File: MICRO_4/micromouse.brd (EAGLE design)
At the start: 100 x 80 mm, 33 parts

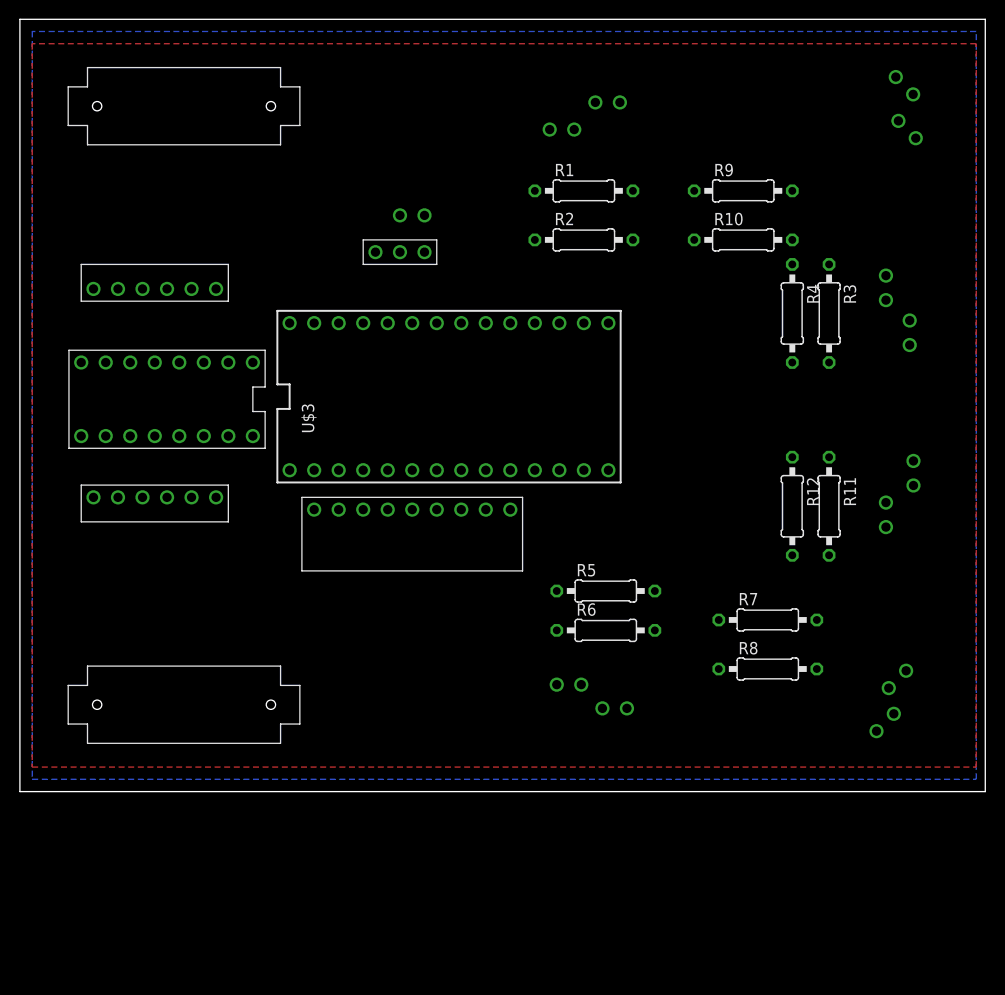
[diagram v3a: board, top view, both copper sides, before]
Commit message: all the traces on top layer alone next will include bottom layer for traces
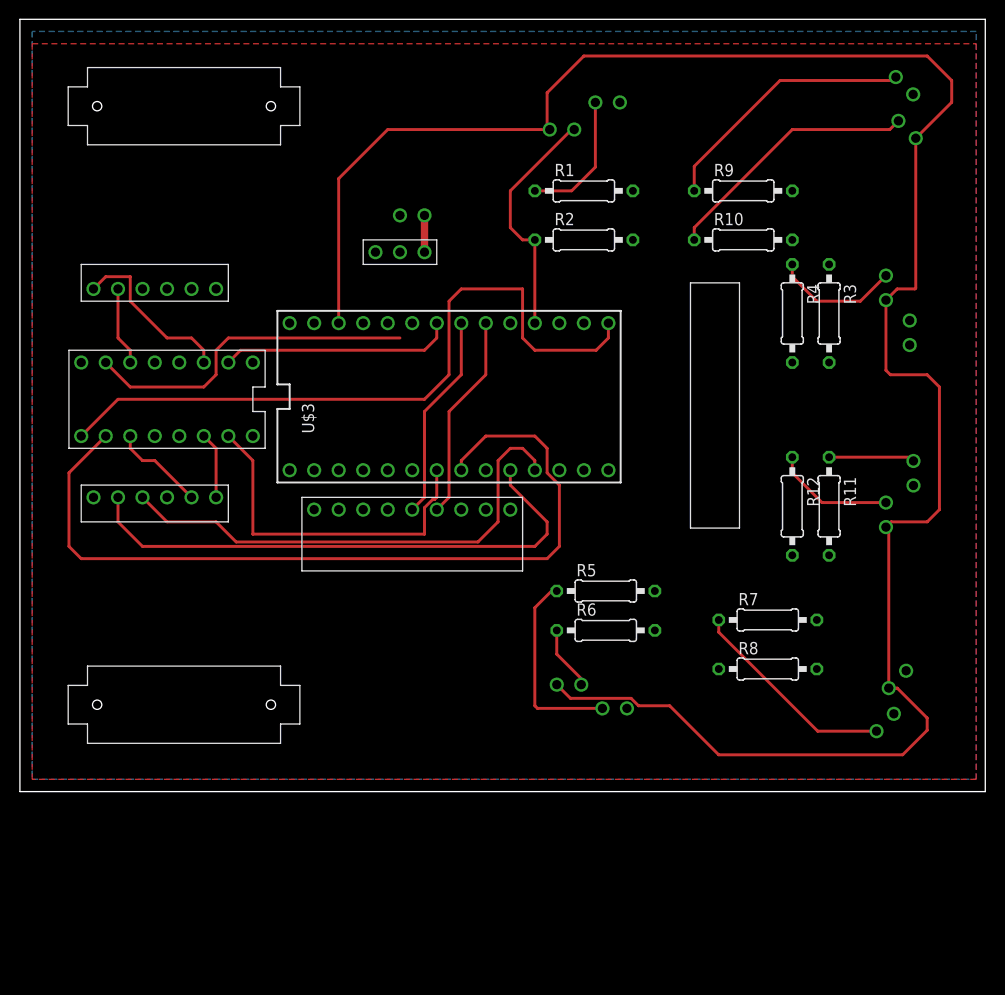
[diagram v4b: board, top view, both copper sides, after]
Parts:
- added U$20: BALL_CASTER, BALL_CASTER:BALL_CASTER
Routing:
- net 3.3V_VCC: track 0.00 -> 212.2 mm
- net M2_FWD_PWM: track 0.00 -> 87.0 mm
- net M2_ENABLE: track 0.00 -> 73.1 mm
- net OUTB_R: track 0.00 -> 56.8 mm
- net OUTA_R: track 0.00 -> 51.8 mm
- net N$5: track 0.00 -> 36.3 mm
- net M1_REV_PWM: track 0.00 -> 35.1 mm
- net N$10: track 0.00 -> 27.3 mm
- net N$12: track 0.00 -> 27.0 mm
- net N$28: track 0.00 -> 24.7 mm
- net M1_FWD_PWM: track 0.00 -> 24.2 mm
- net N$7: track 0.00 -> 21.9 mm
- net N$3: track 0.00 -> 21.4 mm
- net N$2: track 0.00 -> 21.4 mm
- net N$26: track 0.00 -> 20.3 mm
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- added copper zone on layer 1, net 5V_VCC
- removed copper zone on layer 1, net 3.3V_VCC

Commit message: all routes are traced
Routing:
- net N$8: track 0.00 -> 95.2 mm, vias 0 -> 5
- net N$22: track 0.00 -> 74.3 mm, vias 0 -> 6
- net N$4: track 0.00 -> 65.9 mm, vias 0 -> 4
- net N$19: track 0.00 -> 61.6 mm, vias 0 -> 3
- net OUTB_L: track 0.00 -> 57.2 mm, vias 0 -> 4
- net N$9: track 0.00 -> 56.4 mm, vias 0 -> 6
- net N$6: track 0.00 -> 53.9 mm, vias 0 -> 2
- net OUTA_L: track 0.00 -> 52.0 mm, vias 0 -> 4
- net N$14: track 12.6 -> 61.9 mm, vias 0 -> 1
- net N$12: track 27.0 -> 75.1 mm, vias 0 -> 2
- net N$11: track 0.00 -> 46.4 mm, vias 0 -> 1
- net N$25: track 0.00 -> 43.4 mm, vias 0 -> 2
- net N$21: track 6.67 -> 44.9 mm, vias 0 -> 3
- net N$24: track 13.1 -> 46.6 mm, vias 0 -> 1
- net N$23: track 0.00 -> 10.8 mm
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
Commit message: made more space for motors
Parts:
- moved U$1 3.81 mm to (16.5, 47.0)
- moved U$2 2.54 mm to (11.4, 34.3)
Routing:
- net M1_L: track 17.9 -> 22.5 mm
- net M2_L: track 8.15 -> 4.34 mm
- net OUTB_R: track 56.8 -> 59.3 mm
- net M1_R: track 6.88 -> 4.34 mm
- net OUTA_R: track 51.8 -> 53.9 mm
- net M2_R: track 9.72 -> 8.35 mm
- net OUTB_L: track 57.2 -> 58.2 mm
- net OUTA_L: track 52.0 -> 51.8 mm, vias 4 -> 6
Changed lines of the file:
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@@
 <setting verticaltext="up"/>
 </settings>
-<grid distance="50" unitdist="mil" unit="mil" style="lines" multiple="1" display="yes" altdistance="5" altunitdist="mil" altunit="mil"/>
+<grid distance="1" unitdist="mm" unit="mm" style="lines" multiple="1" display="yes" altdistance="5" altunitdist="mil" altunit="mil"/>
 <layers>
 <layer number="1" name="Top" color="4" fill="1" visible="yes" active="yes"/>
@@
 <attribute name="SPICEPREFIX" value="R" x="74.93" y="62.23" size="1.778" layer="27" display="off"/>
 </element>
-<element name="U$1" library="MOTOR_ENCODER" package="MOTOR_ENCODER" value="MOTOR_ENCODER" x="16.51" y="50.8" rot="R270"/>
+<element name="U$1" library="MOTOR_ENCODER" package="MOTOR_ENCODER" value="MOTOR_ENCODER" x="16.51" y="46.99" rot="R270"/>
 <element name="U$10" library="VOLTAGE_REGULATOR" package="VOLTAGE_REGULATOR" value="VOLTAGE_REGULATOR" x="39.37" y="55.88"/>
 <element name="U$11" library="Battery_input" package="BATTERY_INPUT" value="BATTERY_INPUT" x="40.64" y="59.69" rot="R180"/>
@@
 <element name="U$16" library="IR_EMITTER" package="IR_EMITTER" value="IR_EMITTER" x="91.63" y="73.12" rot="R315"/>
 <element name="U$17" library="IR_RECIEVER" package="IR_RECIEVER" value="IR_RECIEVER" x="91.9" y="68.58" rot="R135"/>
-<element name="U$2" library="MOTOR_ENCODER" package="MOTOR_ENCODER" value="MOTOR_ENCODER" x="11.43" y="31.75" rot="R90"/>
+<element name="U$2" library="MOTOR_ENCODER" package="MOTOR_ENCODER" value="MOTOR_ENCODER" x="11.43" y="34.29" rot="R90"/>
 <element name="U$22" library="IR_EMITTER" package="IR_EMITTER" value="IR_EMITTER" x="92.56" y="32.98" rot="R270"/>
 <element name="U$23" library="IR_RECIEVER" package="IR_RECIEVER" value="IR_RECIEVER" x="89.71" y="28.67" rot="R90"/>
@@
 <contactref element="U$4" pad="L_M1_1"/>
 <contactref element="U$1" pad="M1"/>
-<wire x1="7.62" y1="52.07" x2="8.89" y2="53.34" width="0.3048" layer="1"/>
+<wire x1="7.62" y1="48.26" x2="8.89" y2="53.34" width="0.3048" layer="1"/>
 <wire x1="8.89" y1="53.34" x2="11.43" y2="53.34" width="0.3048" layer="1"/>
 <wire x1="11.43" y1="53.34" x2="11.43" y2="50.8" width="0.3048" layer="1"/>
-<wire x1="15.24" y1="46.99" x2="17.78" y2="46.99" width="0.3048" layer="1"/>
 <wire x1="17.78" y1="46.99" x2="19.05" y2="45.72" width="0.3048" layer="1"/>
 <wire x1="19.05" y1="45.72" x2="19.05" y2="44.45" width="0.3048" layer="1"/>
-<wire x1="11.43" y1="50.8" x2="15.24" y2="46.99" width="0.3048" layer="1"/>
+<wire x1="11.43" y1="50.8" x2="12.23" y2="50" width="0.3048" layer="1"/>
+<wire x1="12.23" y1="50" x2="14" y2="50" width="0.3048" layer="1"/>
+<wire x1="14" y1="50" x2="14" y2="48" width="0.3048" layer="1"/>
+<wire x1="14" y1="48" x2="15.01" y2="46.99" width="0.3048" layer="1"/>
+<wire x1="15.01" y1="46.99" x2="17.78" y2="46.99" width="0.3048" layer="1"/>
 </signal>
 <signal name="M2_L">
 <contactref element="U$4" pad="L_M1_2"/>
 <contactref element="U$1" pad="M2"/>
-<wire x1="10.16" y1="52.07" x2="10.16" y2="46.99" width="0.3048" layer="1"/>
+<wire x1="10.16" y1="48.26" x2="10.16" y2="46.99" width="0.3048" layer="1"/>
 <wire x1="10.16" y1="46.99" x2="11.43" y2="45.72" width="0.3048" layer="1"/>
 <wire x1="11.43" y1="45.72" x2="11.43" y2="44.45" width="0.3048" layer="1"/>
@@
 <contactref element="U$2" pad="M1"/>
 <wire x1="19.05" y1="36.83" x2="20.32" y2="35.56" width="0.3048" layer="1"/>
-<wire x1="20.32" y1="35.56" x2="20.32" y2="30.48" width="0.3048" layer="1"/>
+<wire x1="20.32" y1="35.56" x2="20.32" y2="33.02" width="0.3048" layer="1"/>
 </signal>
 <signal name="M2_R">
@@
 <wire x1="12.7" y1="34.29" x2="11.43" y2="35.56" width="0.3048" layer="1"/>
 <wire x1="11.43" y1="35.56" x2="11.43" y2="36.83" width="0.3048" layer="1"/>
-<wire x1="17.78" y1="30.48" x2="13.97" y2="34.29" width="0.3048" layer="1"/>
+<wire x1="17.78" y1="33.02" x2="13.97" y2="34.29" width="0.3048" layer="1"/>
 </signal>
 <signal name="N$4">
@@
 <contactref element="U$1" pad="OUTA"/>
 <contactref element="U$3" pad="10"/>
-<wire x1="15.24" y1="52.07" x2="19.05" y2="48.26" width="0.3048" layer="1"/>
-<wire x1="19.05" y1="48.26" x2="25.4" y2="48.26" width="0.3048" layer="1"/>
 <via x="25.4" y="48.26" extent="1-16" drill="0.35"/>
 <wire x1="25.4" y1="48.26" x2="29.21" y2="44.45" width="0.3048" layer="16"/>
@@
 <wire x1="53.34" y1="41.91" x2="55.88" y2="39.37" width="0.3048" layer="1"/>
 <wire x1="55.88" y1="39.37" x2="55.88" y2="33.29" width="0.3048" layer="1"/>
+<wire x1="15.24" y1="48.26" x2="15.26" y2="48.26" width="0.3048" layer="1"/>
+<wire x1="15.26" y1="48.26" x2="17" y2="50" width="0.3048" layer="1"/>
+<via x="17" y="50" extent="1-16" drill="0.35"/>
+<wire x1="17" y1="50" x2="21" y2="50" width="0.3048" layer="16"/>
+<via x="21" y="50" extent="1-16" drill="0.35"/>
+<wire x1="21" y1="50" x2="23.66" y2="50" width="0.3048" layer="1"/>
+<wire x1="23.66" y1="50" x2="25.4" y2="48.26" width="0.3048" layer="1"/>
 </signal>
 <signal name="OUTB_L">
 <contactref element="U$1" pad="OUTB"/>
 <contactref element="U$3" pad="11"/>
-<wire x1="17.78" y1="52.07" x2="19.05" y2="50.8" width="0.3048" layer="1"/>
+<wire x1="17.78" y1="48.26" x2="19.05" y2="50.8" width="0.3048" layer="1"/>
 <wire x1="19.05" y1="50.8" x2="31.75" y2="50.8" width="0.3048" layer="1"/>
 <wire x1="31.75" y1="50.8" x2="31.75" y2="48.26" width="0.3048" layer="1"/>
@@
 <contactref element="U$2" pad="OUTB"/>
 <contactref element="U$3" pad="8"/>
-<wire x1="10.16" y1="30.48" x2="10.16" y2="27.94" width="0.3048" layer="1"/>
+<wire x1="10.16" y1="33.02" x2="10.16" y2="27.94" width="0.3048" layer="1"/>
 <wire x1="12.7" y1="25.4" x2="53.34" y2="25.4" width="0.3048" layer="1"/>
 <wire x1="53.34" y1="25.4" x2="54.61" y2="26.67" width="0.3048" layer="1"/>
@@
 <contactref element="U$2" pad="OUTA"/>
 <contactref element="U$3" pad="9"/>
-<wire x1="12.7" y1="30.48" x2="15.24" y2="27.94" width="0.3048" layer="1"/>
+<wire x1="12.7" y1="33.02" x2="15.24" y2="27.94" width="0.3048" layer="1"/>
 <wire x1="15.24" y1="27.94" x2="20.32" y2="27.94" width="0.3048" layer="1"/>
 <wire x1="20.32" y1="27.94" x2="22.4028" y2="25.8572" width="0.3048" layer="1"/>

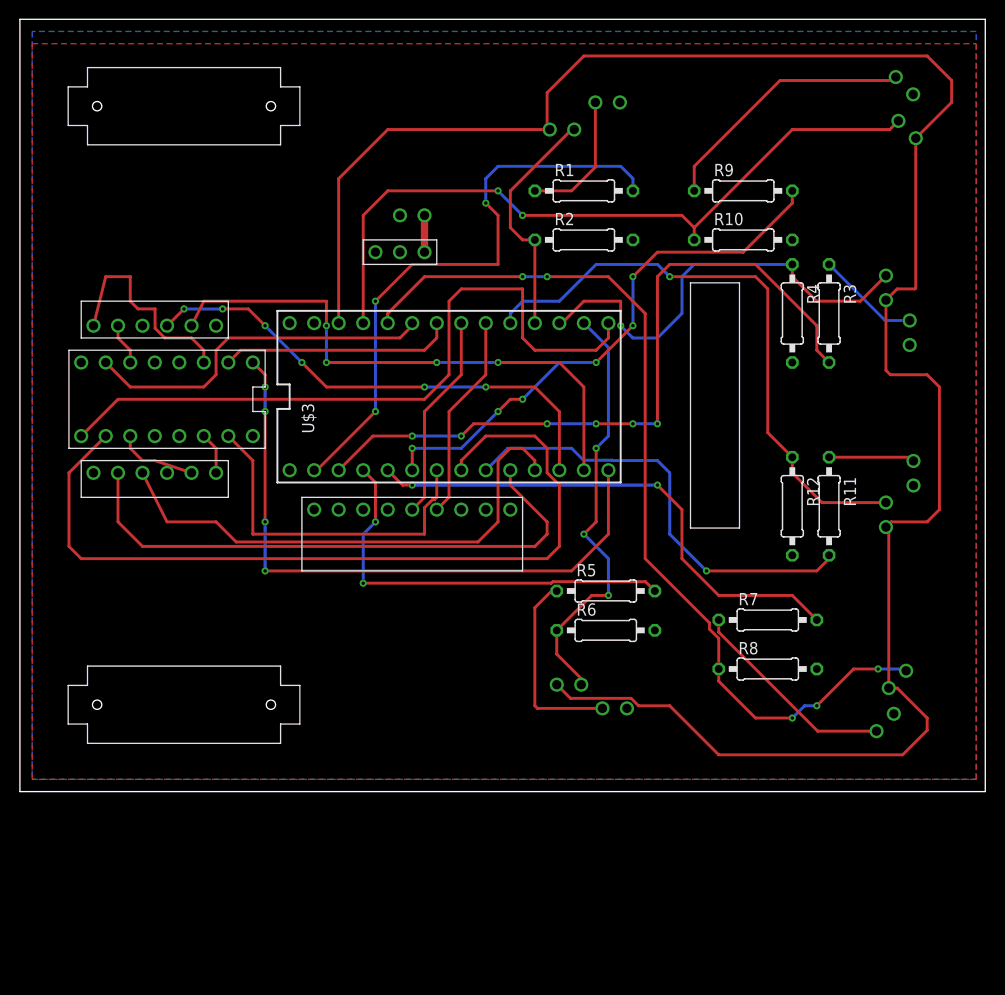
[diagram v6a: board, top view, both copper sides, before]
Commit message: made more space for ir's so they can fit onto the board
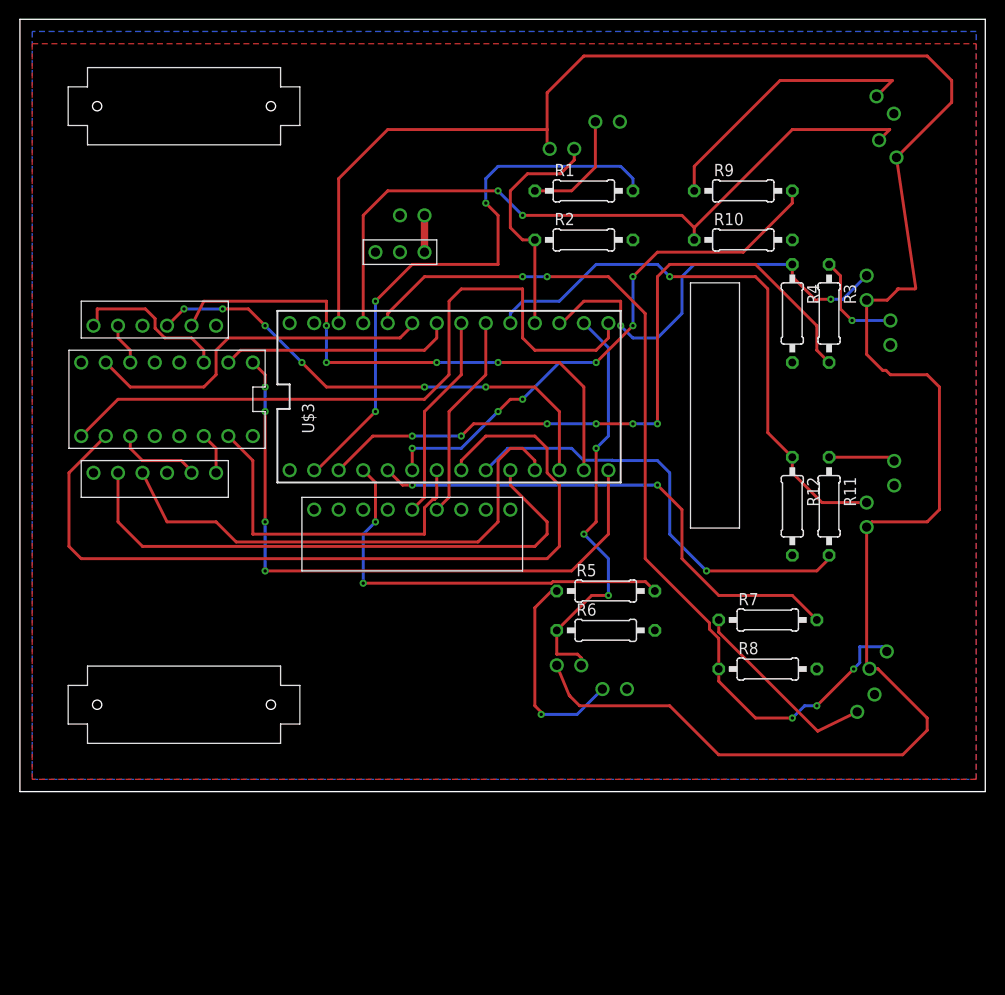
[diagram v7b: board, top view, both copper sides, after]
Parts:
- moved U$14 2.83 mm to (87.6, 9.16)
- moved U$15 2.83 mm to (88.9, 13.6)
- moved U$16 2.83 mm to (89.6, 71.1)
- moved U$17 2.83 mm to (89.9, 66.6)
- moved U$12 2.00 mm to (87.7, 52.2)
- moved U$22 2.00 mm to (90.6, 33.0)
- moved U$23 2.00 mm to (87.7, 28.7)
- moved U$5 2.00 mm to (56.1, 66.6)
- moved U$6 2.00 mm to (90.2, 47.5)
- moved U$7 2.00 mm to (61.6, 10.6)
- moved U$8 2.00 mm to (56.9, 13.1)
- moved U$9 2.00 mm to (60.9, 69.4)
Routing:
- net 3.3V_VCC: track 212.2 -> 222.6 mm
- net M1_L: track 22.5 -> 16.6 mm
- net N$14: track 61.9 -> 59.9 mm
- net N$20: track 14.0 -> 12.0 mm
- net N$13: track 8.90 -> 6.90 mm
- net N$24: track 46.6 -> 44.6 mm, vias 1 -> 2
- net N$10: track 27.3 -> 29.1 mm
- net N$7: track 21.9 -> 20.3 mm
- net N$26: track 20.3 -> 21.7 mm, vias 0 -> 1
- net N$21: track 44.9 -> 44.1 mm
- net N$23: vias 0 -> 1
